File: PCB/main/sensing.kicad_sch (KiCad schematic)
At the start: 0 parts

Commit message: Add notes
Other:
- company: (none) -> University of Cape Town
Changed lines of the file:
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@@
     (date "2022-03-09")
     (rev "v1.0")
+    (company "University of Cape Town")
+    (comment 4 "Authors: Heather WImberley")
   )
   (text "Sensors and supporting analog components, decoupling, pin assignments"

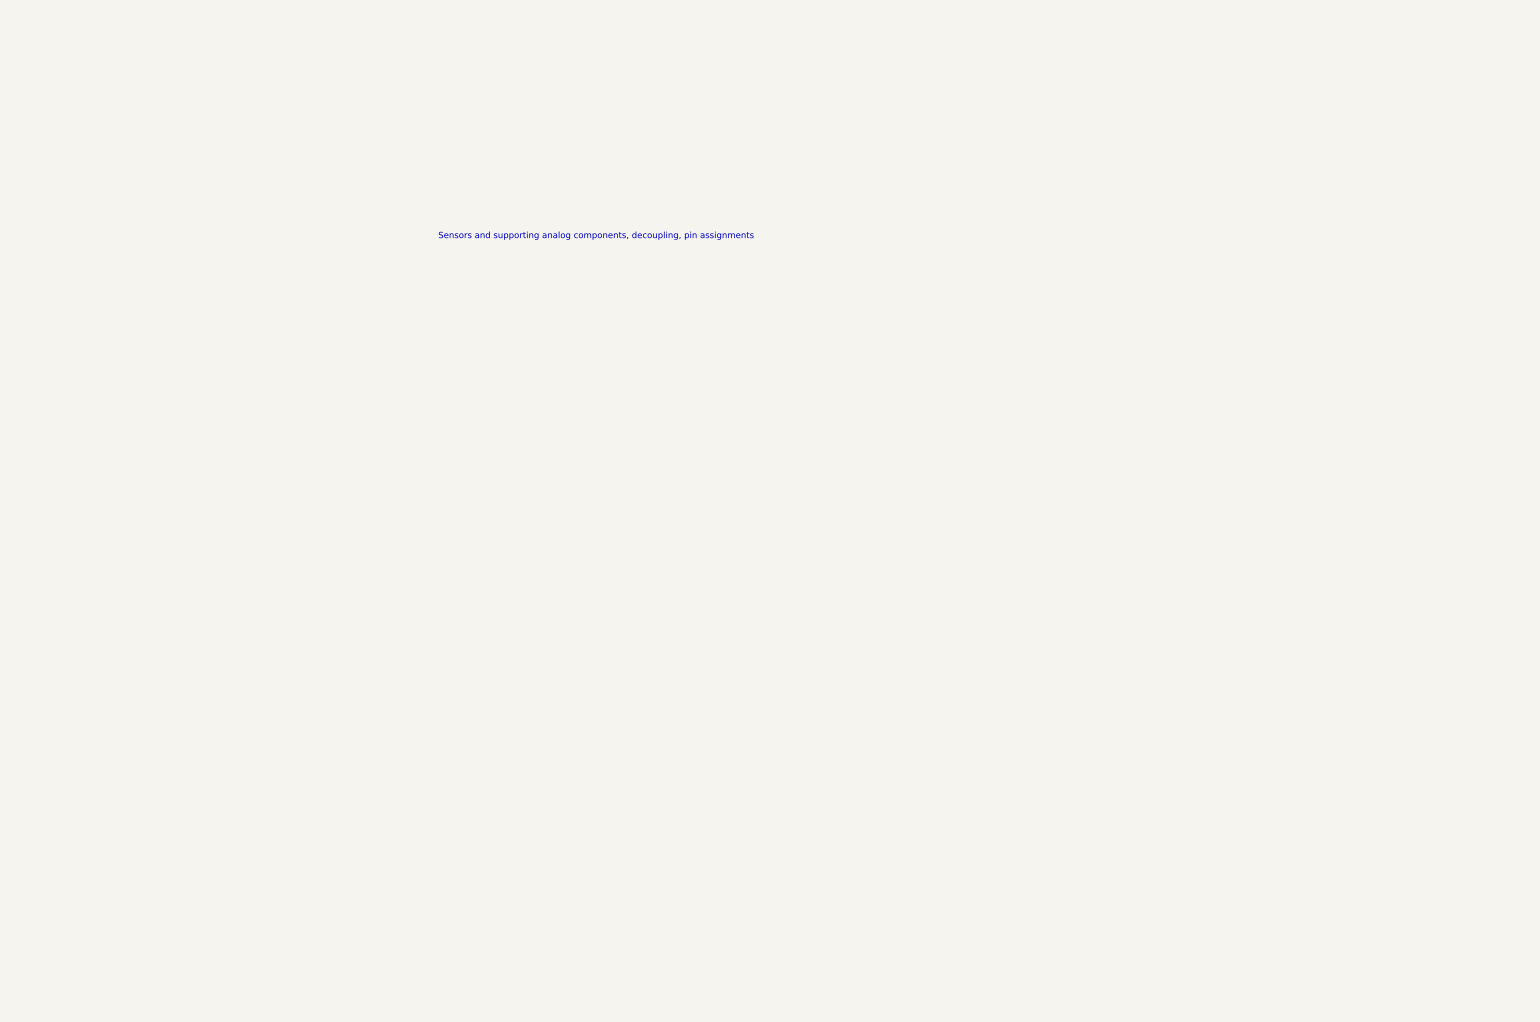
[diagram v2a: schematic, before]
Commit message: Added Sensing Schematics
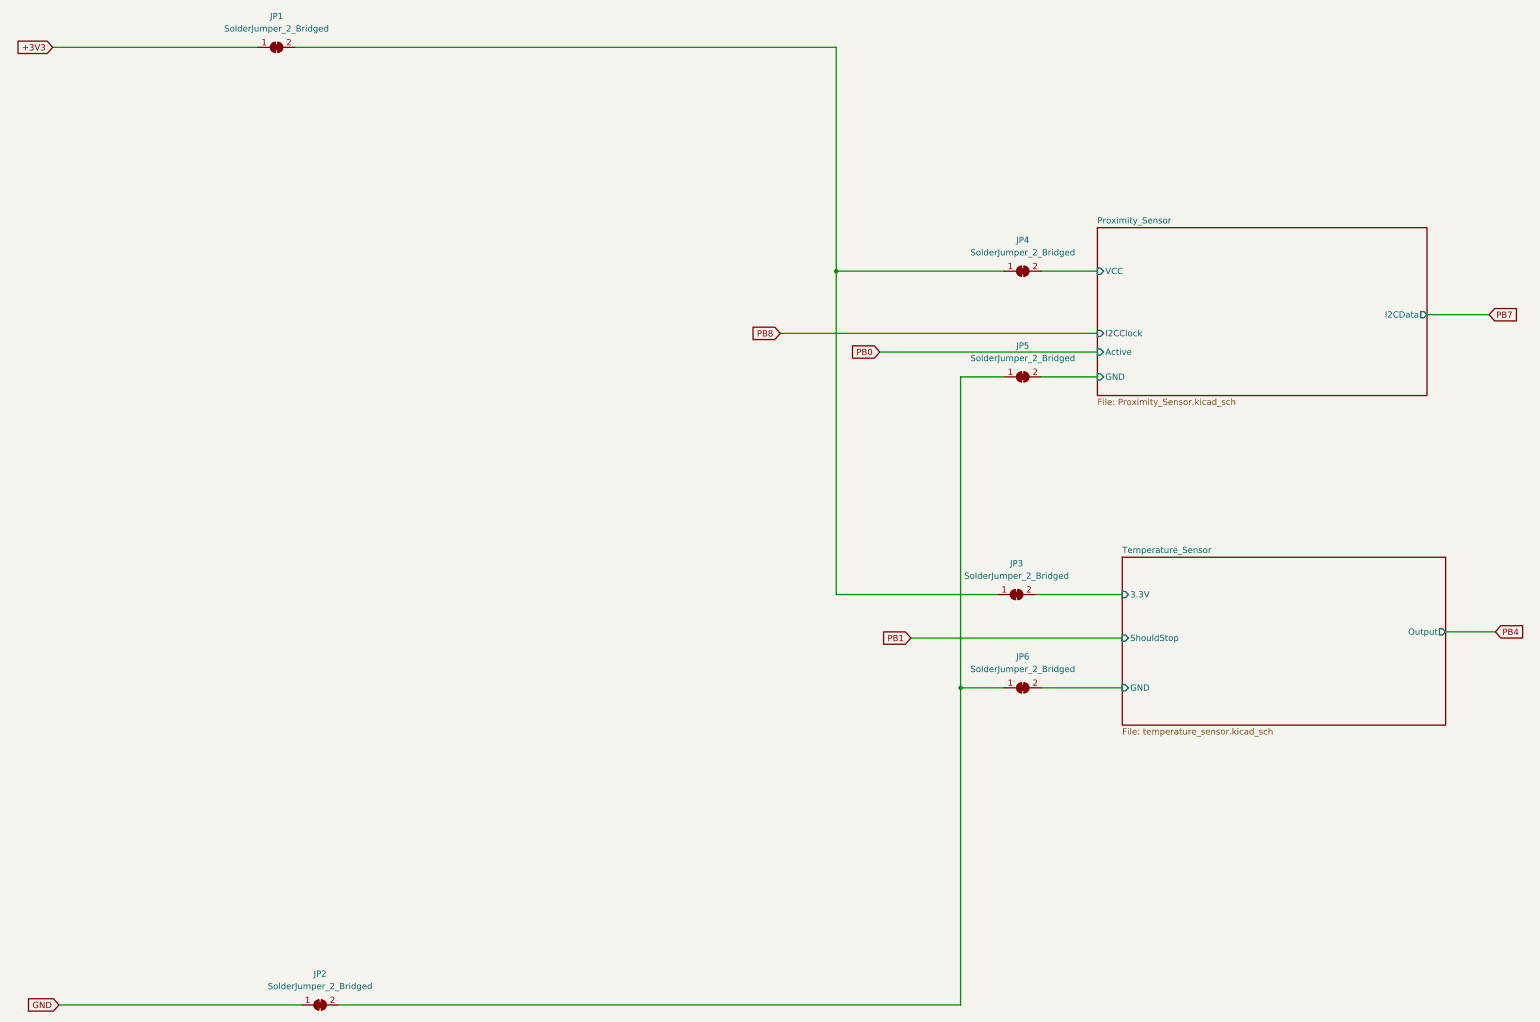
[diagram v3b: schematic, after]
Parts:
- added JP1, JP2, JP3, JP4, JP5, JP6: SolderJumper_2_Bridged, symbol Jumper:SolderJumper_2_Bridged
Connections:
- new net: JP1.2 (B), JP3.1 (A), JP4.1 (A)
- new net: JP2.2 (B), JP5.1 (A), JP6.1 (A)
- new net +3V3: JP1.1 (A)
- new net GND: JP2.1 (A)
- new net Proximity_Sensor/GND: JP5.2 (B)
- new net Proximity_Sensor/VCC: JP4.2 (B)
- new net Temperature_Sensor/3.3V: JP3.2 (B)
- new net Temperature_Sensor/GND: JP6.2 (B)
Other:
- added sheet Proximity_Sensor (Proximity_Sensor.kicad_sch)
- added sheet Temperature_Sensor (temperature_sensor.kicad_sch)
- note removed: "Sensors and supporting analog components, decoupling, pin assignments"
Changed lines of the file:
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@@
 (kicad_sch (version 20211123) (generator eeschema)
-  (paper "A4")
+  (paper "A3")
   (title_block
     (date "2022-03-09")
@@
     (comment 4 "Authors: Heather WImberley")
   )
-  (text "Sensors and supporting analog components, decoupling, pin assignments"
-    (at 115.57 86.36 0)
-    (effects (font (size 1.27 1.27)) (justify left bottom))
+  (junction (at 222.25 177.8) (diameter 0) (color 0 0 0 0)
+  )
+  (junction (at 196.85 92.71) (diameter 0) (color 0 0 0 0)
+  )
+  (wire (pts (xy 321.31 166.37) (xy 331.47 166.37))
+    (stroke (width 0) (type default) (color 0 0 0 0))
+  )
+  (wire (pts (xy 222.25 177.8) (xy 222.25 114.3))
+    (stroke (width 0) (type default) (color 0 0 0 0))
+  )
+  (wire (pts (xy 222.25 242.57) (xy 222.25 177.8))
+    (stroke (width 0) (type default) (color 0 0 0 0))
+  )
+  (wire (pts (xy 238.76 177.8) (xy 255.27 177.8))
+    (stroke (width 0) (type default) (color 0 0 0 0))
+  )
+  (wire (pts (xy 238.76 92.71) (xy 250.19 92.71))
+    (stroke (width 0) (type default) (color 0 0 0 0))
+  )
+  (wire (pts (xy 185.42 105.41) (xy 250.19 105.41))
+    (stroke (width 0) (type default) (color 0 0 0 0))
+  )
+  (wire (pts (xy 212.09 167.64) (xy 255.27 167.64))
+    (stroke (width 0) (type default) (color 0 0 0 0))
+  )
+  (wire (pts (xy 317.5 101.6) (xy 330.2 101.6))
+    (stroke (width 0) (type default) (color 0 0 0 0))
+  )
+  (wire (pts (xy 86.36 46.99) (xy 196.85 46.99))
+    (stroke (width 0) (type default) (color 0 0 0 0))
+  )
+  (wire (pts (xy 196.85 158.75) (xy 196.85 92.71))
+    (stroke (width 0) (type default) (color 0 0 0 0))
+  )
+  (wire (pts (xy 36.83 46.99) (xy 78.74 46.99))
+    (stroke (width 0) (type default) (color 0 0 0 0))
+  )
+  (wire (pts (xy 229.87 158.75) (xy 196.85 158.75))
+    (stroke (width 0) (type default) (color 0 0 0 0))
+  )
+  (wire (pts (xy 38.1 242.57) (xy 87.63 242.57))
+    (stroke (width 0) (type default) (color 0 0 0 0))
+  )
+  (wire (pts (xy 222.25 114.3) (xy 231.14 114.3))
+    (stroke (width 0) (type default) (color 0 0 0 0))
+  )
+  (wire (pts (xy 237.49 158.75) (xy 255.27 158.75))
+    (stroke (width 0) (type default) (color 0 0 0 0))
+  )
+  (wire (pts (xy 196.85 92.71) (xy 196.85 46.99))
+    (stroke (width 0) (type default) (color 0 0 0 0))
+  )
+  (wire (pts (xy 95.25 242.57) (xy 222.25 242.57))
+    (stroke (width 0) (type default) (color 0 0 0 0))
+  )
+  (wire (pts (xy 222.25 177.8) (xy 231.14 177.8))
+    (stroke (width 0) (type default) (color 0 0 0 0))
+  )
+  (wire (pts (xy 196.85 92.71) (xy 231.14 92.71))
+    (stroke (width 0) (type default) (color 0 0 0 0))
+  )
+  (wire (pts (xy 205.74 109.22) (xy 250.19 109.22))
+    (stroke (width 0) (type default) (color 0 0 0 0))
+  )
+  (wire (pts (xy 238.76 114.3) (xy 250.19 114.3))
+    (stroke (width 0) (type default) (color 0 0 0 0))
+  )
+  (global_label "PB8" (shape input) (at 185.42 105.41 180) (fields_autoplaced)
+    (effects (font (size 1.27 1.27)) (justify right))
+    (property "Intersheet References" "${INTERSHEET_REFS}" (id 0) (at 179.2574 105.3306 0)
+      (effects (font (size 1.27 1.27)) (justify right) hide)
+    )
+  )
+  (global_label "PB7" (shape input) (at 330.2 101.6 0) (fields_autoplaced)
+    (effects (font (size 1.27 1.27)) (justify left))
+    (property "Intersheet References" "${INTERSHEET_REFS}" (id 0) (at 336.3626 101.5206 0)
+      (effects (font (size 1.27 1.27)) (justify left) hide)
+    )
+  )
+  (global_label "+3V3" (shape input) (at 36.83 46.99 180) (fields_autoplaced)
+    (effects (font (size 1.27 1.27)) (justify right))
+    (property "Intersheet References" "${INTERSHEET_REFS}" (id 0) (at 29.3369 46.9106 0)
+      (effects (font (size 1.27 1.27)) (justify right) hide)
+    )
+  )
+  (global_label "GND" (shape input) (at 38.1 242.57 180) (fields_autoplaced)
+    (effects (font (size 1.27 1.27)) (justify right))
+    (property "Intersheet References" "${INTERSHEET_REFS}" (id 0) (at 31.8164 242.4906 0)
+      (effects (font (size 1.27 1.27)) (justify right) hide)
+    )
+  )
+  (global_label "PB4" (shape input) (at 331.47 166.37 0) (fields_autoplaced)
+    (effects (font (size 1.27 1.27)) (justify left))
+    (property "Intersheet References" "${INTERSHEET_REFS}" (id 0) (at 337.6326 166.2906 0)
+      (effects (font (size 1.27 1.27)) (justify left) hide)
+    )
+  )
+  (global_label "PB0" (shape input) (at 205.74 109.22 180) (fields_autoplaced)
+    (effects (font (size 1.27 1.27)) (justify right))
+    (property "Intersheet References" "${INTERSHEET_REFS}" (id 0) (at 199.5774 109.2994 0)
+      (effects (font (size 1.27 1.27)) (justify right) hide)
+    )
+  )
+  (global_label "PB1" (shape input) (at 212.09 167.64 180) (fields_autoplaced)
+    (effects (font (size 1.27 1.27)) (justify right))
+    (property "Intersheet References" "${INTERSHEET_REFS}" (id 0) (at 205.9274 167.7194 0)
+      (effects (font (size 1.27 1.27)) (justify right) hide)
+    )
+  )
+  (symbol (lib_id "Jumper:SolderJumper_2_Bridged") (at 234.95 92.71 0) (unit 1)
+    (in_bom yes) (on_board yes) (fields_autoplaced)
+    (property "Reference" "JP4" (id 0) (at 234.95 86.36 0))
+    (property "Value" "SolderJumper_2_Bridged" (id 1) (at 234.95 88.9 0))
+    (property "Footprint" "" (id 2) (at 234.95 92.71 0)
+      (effects (font (size 1.27 1.27)) hide)
+    )
+    (property "Datasheet" "~" (id 3) (at 234.95 92.71 0)
+      (effects (font (size 1.27 1.27)) hide)
+    )
+    (pin "1")
+    (pin "2")
+  )
+  (symbol (lib_id "Jumper:SolderJumper_2_Bridged") (at 234.95 177.8 0) (unit 1)
+    (in_bom yes) (on_board yes) (fields_autoplaced)
+    (property "Reference" "JP6" (id 0) (at 234.95 171.45 0))
+    (property "Value" "SolderJumper_2_Bridged" (id 1) (at 234.95 173.99 0))
+    (property "Footprint" "" (id 2) (at 234.95 177.8 0)
+      (effects (font (size 1.27 1.27)) hide)
+    )
+    (property "Datasheet" "~" (id 3) (at 234.95 177.8 0)
+      (effects (font (size 1.27 1.27)) hide)
+    )
+    (pin "1")
+    (pin "2")
+  )
+  (symbol (lib_id "Jumper:SolderJumper_2_Bridged") (at 233.68 158.75 0) (unit 1)
+    (in_bom yes) (on_board yes) (fields_autoplaced)
+    (property "Reference" "JP3" (id 0) (at 233.68 152.4 0))
+    (property "Value" "SolderJumper_2_Bridged" (id 1) (at 233.68 154.94 0))
+    (property "Footprint" "" (id 2) (at 233.68 158.75 0)
+      (effects (font (size 1.27 1.27)) hide)
+    )
+    (property "Datasheet" "~" (id 3) (at 233.68 158.75 0)
+      (effects (font (size 1.27 1.27)) hide)
+    )
+    (pin "1")
+    (pin "2")
+  )
+  (symbol (lib_id "Jumper:SolderJumper_2_Bridged") (at 91.44 242.57 0) (unit 1)
+    (in_bom yes) (on_board yes) (fields_autoplaced)
+    (property "Reference" "JP2" (id 0) (at 91.44 236.22 0))
+    (property "Value" "SolderJumper_2_Bridged" (id 1) (at 91.44 238.76 0))
+    (property "Footprint" "" (id 2) (at 91.44 242.57 0)
+      (effects (font (size 1.27 1.27)) hide)
+    )
+    (property "Datasheet" "~" (id 3) (at 91.44 242.57 0)
+      (effects (font (size 1.27 1.27)) hide)
+    )
+    (pin "1")
+    (pin "2")
+  )
+  (symbol (lib_id "Jumper:SolderJumper_2_Bridged") (at 234.95 114.3 0) (unit 1)
+    (in_bom yes) (on_board yes) (fields_autoplaced)
+    (property "Reference" "JP5" (id 0) (at 234.95 107.95 0))
+    (property "Value" "SolderJumper_2_Bridged" (id 1) (at 234.95 110.49 0))
+    (property "Footprint" "" (id 2) (at 234.95 114.3 0)
+      (effects (font (size 1.27 1.27)) hide)
+    )
+    (property "Datasheet" "~" (id 3) (at 234.95 114.3 0)
+      (effects (font (size 1.27 1.27)) hide)
+    )
+    (pin "1")
+    (pin "2")
+  )
+  (symbol (lib_id "Jumper:SolderJumper_2_Bridged") (at 82.55 46.99 0) (unit 1)
+    (in_bom yes) (on_board yes) (fields_autoplaced)
+    (property "Reference" "JP1" (id 0) (at 82.55 40.64 0))
+    (property "Value" "SolderJumper_2_Bridged" (id 1) (at 82.55 43.18 0))
+    (property "Footprint" "" (id 2) (at 82.55 46.99 0)
+      (effects (font (size 1.27 1.27)) hide)
+    )
+    (property "Datasheet" "~" (id 3) (at 82.55 46.99 0)
+      (effects (font (size 1.27 1.27)) hide)
+    )
+    (pin "1")
+    (pin "2")
+  )
+  (sheet (at 250.19 83.82) (size 67.31 34.29) (fields_autoplaced)
+    (stroke (width 0.1524) (type solid) (color 0 0 0 0))
+    (fill (color 0 0 0 0.0000))
+    (property "Sheet name" "Proximity_Sensor" (id 0) (at 250.19 83.1084 0)
+      (effects (font (size 1.27 1.27)) (justify left bottom))
+    )
+    (property "Sheet file" "Proximity_Sensor.kicad_sch" (id 1) (at 250.19 118.6946 0)
+      (effects (font (size 1.27 1.27)) (justify left top))
+    )
+    (pin "VCC" input (at 250.19 92.71 180)
+      (effects (font (size 1.27 1.27)) (justify left))
+    )
+    (pin "Active" input (at 250.19 109.22 180)
+      (effects (font (size 1.27 1.27)) (justify left))
+    )
+    (pin "GND" input (at 250.19 114.3 180)
+      (effects (font (size 1.27 1.27)) (justify left))
+    )
+    (pin "I2CClock" input (at 250.19 105.41 180)
+      (effects (font (size 1.27 1.27)) (justify left))
+    )
+    (pin "I2CData" output (at 317.5 101.6 0)
+      (effects (font (size 1.27 1.27)) (justify right))
+    )
+  )
+  (sheet (at 255.27 151.13) (size 66.04 34.29) (fields_autoplaced)
+    (stroke (width 0.1524) (type solid) (color 0 0 0 0))
+    (fill (color 0 0 0 0.0000))
+    (property "Sheet name" "Temperature_Sensor" (id 0) (at 255.27 150.4184 0)
+      (effects (font (size 1.27 1.27)) (justify left bottom))
+    )
+    (property "Sheet file" "temperature_sensor.kicad_sch" (id 1) (at 255.27 186.0046 0)
+      (effects (font (size 1.27 1.27)) (justify left top))
+    )
+    (pin "GND" input (at 255.27 177.8 180)
+      (effects (font (size 1.27 1.27)) (justify left))
+    )
+    (pin "Output" output (at 321.31 166.37 0)
+      (effects (font (size 1.27 1.27)) (justify right))
+    )
+    (pin "ShouldStop" input (at 255.27 167.64 180)
+      (effects (font (size 1.27 1.27)) (justify left))
+    )
+    (pin "3.3V" input (at 255.27 158.75 180)
+      (effects (font (size 1.27 1.27)) (justify left))
+    )
   )
 )

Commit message: Add sheet properties
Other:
- title: (none) -> Sensing Submodule
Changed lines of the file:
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@@
   (paper "A3")
   (title_block
+    (title "Sensing Submodule")
     (date "2022-03-09")
     (rev "v1.0")
     (company "University of Cape Town")
-    (comment 4 "Authors: Heather WImberley")
+    (comment 4 "Authors: Kelvin Yankey")
   )
   (junction (at 222.25 177.8) (diameter 0) (color 0 0 0 0)

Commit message: Add changes
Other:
- note added: "Analogue Sensor"
- note added: "Digital Sensor"
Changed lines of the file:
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@@
     (stroke (width 0) (type default) (color 0 0 0 0))
+  )
+  (text "Digital Sensor" (at 271.145 81.28 0)
+    (effects (font (size 3 3) (thickness 0.6) bold) (justify left bottom))
+  )
+  (text "Analogue Sensor" (at 270.51 194.945 0)
+    (effects (font (size 3 3) (thickness 0.6) bold) (justify left bottom))
   )
   (global_label "PB8" (shape input) (at 185.42 105.41 180) (fields_autoplaced)

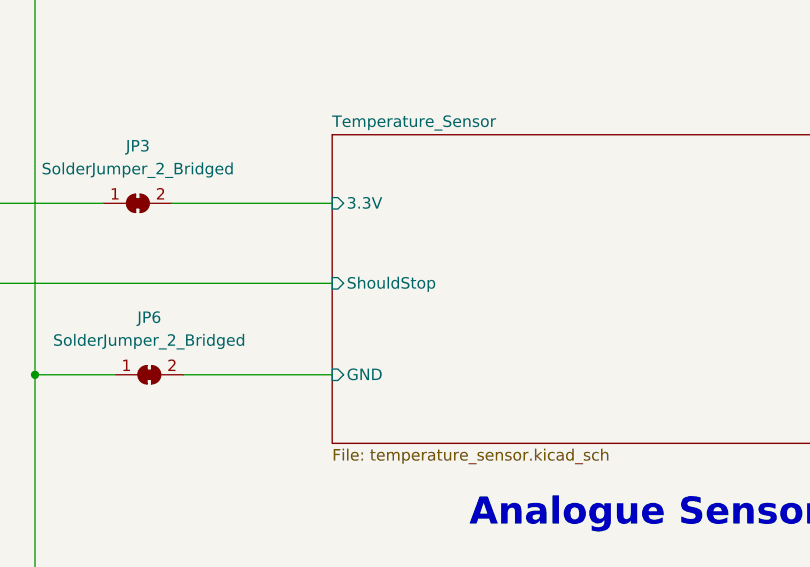
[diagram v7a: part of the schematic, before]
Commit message: Fixed incorrect connection for MOSFET in Sensing Subsystem \n\n Since the BJT switch has been replaced by a MOSFET switch, the Should Stop pin in the temperature sensor should become an Active pin. Indicating when the system should be on
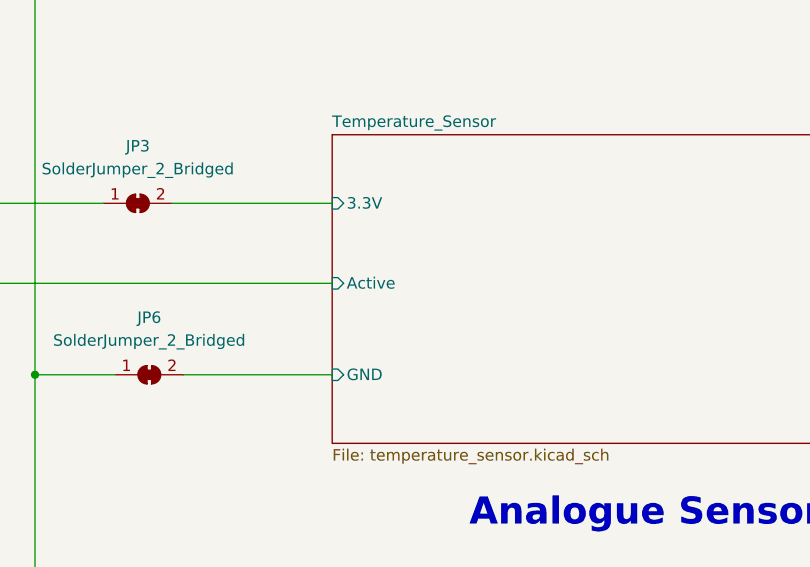
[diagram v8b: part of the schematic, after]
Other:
- sheet Temperature_Sensor ports: added Active; removed ShouldStop
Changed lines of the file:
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@@
       (effects (font (size 1.27 1.27)) (justify right))
-    )
-    (pin "ShouldStop" input (at 255.27 167.64 180)
-      (effects (font (size 1.27 1.27)) (justify left))
     )
     (pin "3.3V" input (at 255.27 158.75 180)
       (effects (font (size 1.27 1.27)) (justify left))
     )
+    (pin "Active" input (at 255.27 167.64 180)
+      (effects (font (size 1.27 1.27)) (justify left))
+    )
